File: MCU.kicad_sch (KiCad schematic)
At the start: 55 parts, among them J701 C5137195, J702 Conn_02x05_Odd_Even, J799 Conn_01x02, SW701 C255807, SW702 C2905169, SW703 C2905169, U610 APS1604M-3SQR-ZR, U703 RP2040, U704 ESP32-S3, U705 W25Q64JVSSIQ, U903 APS1604M-3SQR-SN, Y701 40MHz

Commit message: SUKU mcu positioning and grids fixed, decoupling capacitors placed and routed
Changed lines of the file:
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@@
 		(lib_id "power:+1V1")
 		(at 58.42 165.1 0)
+		(mirror y)
 		(unit 1)
 		(exclude_from_sim no)
@@
 		)
 		(instances
-			(project "grid-devkit-vnsx"
+			(project "grid-devkit"
 				(path "/e5217a0c-7f55-4c30-adda-7f8d95709d1b/00000000-0000-0000-0000-00005d757c78"
 					(page "8")
@@
 		)
 		(instances
-			(project "grid-devkit-vnsx"
+			(project "grid-devkit"
 				(path "/e5217a0c-7f55-4c30-adda-7f8d95709d1b/00000000-0000-0000-0000-00005d757c78"
 					(page "9")

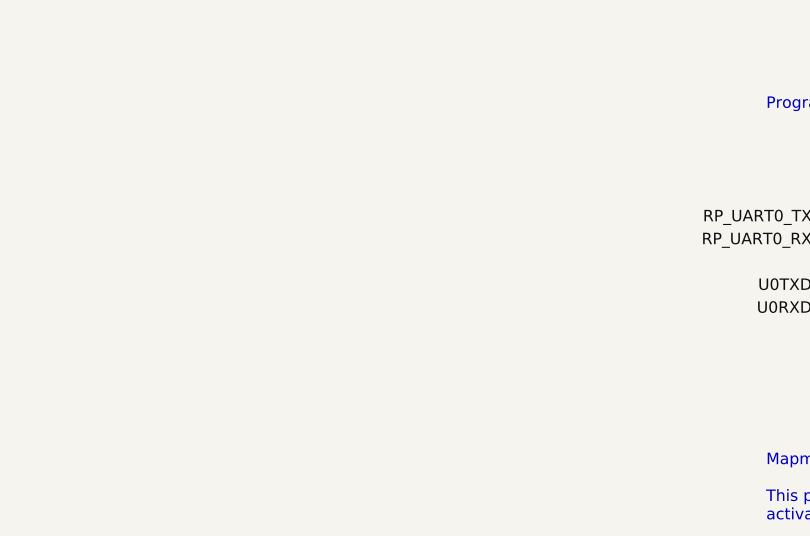
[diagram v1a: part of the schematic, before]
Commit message: SUKU analog layout grid alignment fixed, mcu connection routed
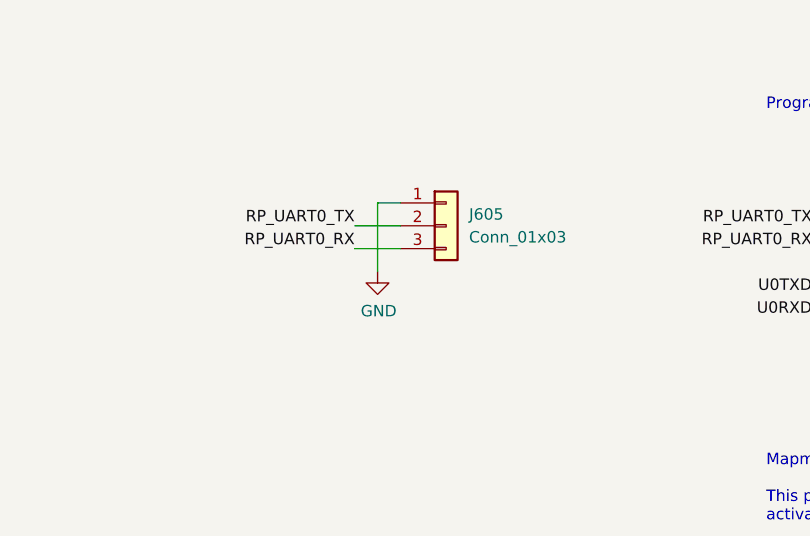
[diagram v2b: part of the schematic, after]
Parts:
- added J605: Conn_01x03, Connector_PinHeader_2.54mm:PinHeader_1x03_P2.54mm_Vertical, symbol Connector_Generic:Conn_01x03
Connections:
- net GND: now also J605.1 (Pin_1)
- net RP_UART0_RX: now also J605.3 (Pin_3)
- net RP_UART0_TX: now also J605.2 (Pin_2)
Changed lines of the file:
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@@
 	(wire
 		(pts
+			(xy 294.64 50.8) (xy 294.64 43.18)
+		)
+		(stroke
+			(width 0)
+			(type default)
+		)
+	)
+	(wire
+		(pts
 			(xy 147.32 38.1) (xy 154.94 38.1)
 		)
@@
 	(wire
 		(pts
+			(xy 292.1 45.72) (xy 297.18 45.72)
+		)
+		(stroke
+			(width 0)
+			(type default)
+		)
+	)
+	(wire
+		(pts
 			(xy 88.9 256.54) (xy 93.98 256.54)
 		)
@@
 	(wire
 		(pts
+			(xy 292.1 48.26) (xy 297.18 48.26)
+		)
+		(stroke
+			(width 0)
+			(type default)
+		)
+	)
+	(wire
+		(pts
 			(xy 147.32 45.72) (xy 147.32 48.26)
 		)
@@
 	(wire
 		(pts
+			(xy 294.64 43.18) (xy 297.18 43.18)
+		)
+		(stroke
+			(width 0)
+			(type default)
+		)
+	)
+	(wire
+		(pts
 			(xy 360.68 132.08) (xy 360.68 134.62)
 		)
@@
 		)
 	)
+	(label "RP_UART0_RX"
+		(at 292.1 48.26 180)
+		(effects
+			(font
+				(size 1.27 1.27)
+			)
+			(justify right bottom)
+		)
+	)
 	(label "GRID_SYNC_1"
 		(at 93.98 251.46 0)
@@
 		)
 	)
+	(label "RP_UART0_TX"
+		(at 292.1 45.72 180)
+		(effects
+			(font
+				(size 1.27 1.27)
+			)
+			(justify right bottom)
+		)
+	)
 	(label "SPICS1"
 		(at 259.08 180.34 180)
@@
 	)
 	(symbol
+		(lib_id "Connector_Generic:Conn_01x03")
+		(at 302.26 45.72 0)
+		(unit 1)
+		(exclude_from_sim no)
+		(in_bom yes)
+		(on_board yes)
+		(dnp no)
+		(fields_autoplaced yes)
+		(property "Reference" "J605"
+			(at 304.8 44.4499 0)
+			(effects
+				(font
+					(size 1.27 1.27)
+				)
+				(justify left)
+			)
+		)
+		(property "Value" "Conn_01x03"
+			(at 304.8 46.9899 0)
+			(effects
+				(font
+					(size 1.27 1.27)
+				)
+				(justify left)
+			)
+		)
+		(property "Footprint" "Connector_PinHeader_2.54mm:PinHeader_1x03_P2.54mm_Vertical"
+			(at 302.26 45.72 0)
+			(effects
+				(font
+					(size 1.27 1.27)
+				)
+				(hide yes)
+			)
+		)
+		(property "Datasheet" "~"
+			(at 302.26 45.72 0)
+			(effects
+				(font
+					(size 1.27 1.27)
+				)
+				(hide yes)
+			)
+		)
+		(property "Description" "Generic connector, single row, 01x03, script generated (kicad-library-utils/schlib/autogen/connector/)"
+			(at 302.26 45.72 0)
+			(effects
+				(font
+					(size 1.27 1.27)
+				)
+				(hide yes)
+			)
+		)
+		(pin "3"
+		)
+		(pin "2"
+		)
+		(pin "1"
+		)
+		(instances
+			(project "grid-devkit"
+				(path "/e5217a0c-7f55-4c30-adda-7f8d95709d1b/00000000-0000-0000-0000-00005d757c78"
+					(reference "J605")
+					(unit 1)
+				)
+			)
+		)
+	)
+	(symbol
 		(lib_name "GND_7")
 		(lib_id "power:GND")
@@
 					(unit 1)
 				)
+			)
+		)
+	)
+	(symbol
+		(lib_name "GND_18")
+		(lib_id "power:GND")
+		(at 294.64 50.8 0)
+		(unit 1)
+		(exclude_from_sim no)
+		(in_bom yes)
+		(on_board yes)
+		(dnp no)
+		(property "Reference" "#PWR0854"
+			(at 294.64 57.15 0)
+			(effects
+				(font
+					(size 1.27 1.27)
+				)
+				(hide yes)
+			)
+		)
+		(property "Value" "GND"
+			(at 294.767 55.1942 0)
+			(effects
+				(font
+					(size 1.27 1.27)
+				)
+			)
+		)
+		(property "Footprint" ""
+			(at 294.64 50.8 0)
+			(effects
+				(font
+					(size 1.27 1.27)
+				)
+				(hide yes)
+			)
+		)
+		(property "Datasheet" ""
+			(at 294.64 50.8 0)
+			(effects
+				(font
+					(size 1.27 1.27)
+				)
+				(hide yes)
+			)
+		)
+		(property "Description" ""
+			(at 294.64 50.8 0)
+			(effects
+				(font
+					(size 1.27 1.27)
+				)
+				(hide yes)
+			)
+		)
+		(pin "1"
+		)
+		(instances
+			(project "grid-devkit"
+				(path "/e5217a0c-7f55-4c30-adda-7f8d95709d1b/00000000-0000-0000-0000-00005d757c78"
+					(reference "#PWR0854")
+					(unit 1)
+				)
